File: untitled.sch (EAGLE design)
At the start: 9 parts, among them IC1 STM32F030F4P, X1 332-02, X2 332-04, X3 332-02, X4 332-02

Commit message: version 0.2
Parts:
- removed SV1: (no value), con-lstb:MA03-1
- added R2: (no value), rcl:R-EU_M1206
- added U1: GY-521MPU6050, gy-521:GY-521MPU6050
- added X5: 332-02, con-garry:332-02
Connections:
- net GND: now also X5-1.S; no longer SV1.1
- net N$10: now also R2.1, X5-2.S; no longer SV1.2
- net VCC: now also R2.2; no longer SV1.3
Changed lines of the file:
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@@
 <part name="SUPPLY5" library="supply2" deviceset="VCC" device=""/>
 <part name="X3" library="con-garry" deviceset="332-02" device=""/>
-<part name="SV1" library="con-lstb" deviceset="MA03-1" device=""/>
 <part name="GND5" library="supply1" deviceset="GND" device=""/>
 <part name="SUPPLY6" library="supply2" deviceset="VCC" device=""/>
 <part name="X4" library="con-garry" deviceset="332-02" device=""/>
 <part name="SUPPLY7" library="supply2" deviceset="VCC" device=""/>
+<part name="U1" library="gy-521" deviceset="GY-521" device="MPU6050"/>
+<part name="R2" library="rcl" deviceset="R-EU_" device="M1206"/>
+<part name="X5" library="con-garry" deviceset="332-02" device=""/>
 </parts>
 <sheets>
@@
 <instance part="X3" gate="-1" x="111.76" y="101.6"/>
 <instance part="X3" gate="-2" x="132.08" y="101.6"/>
-<instance part="SV1" gate="G$1" x="7.62" y="63.5" rot="R90"/>
 <instance part="GND5" gate="1" x="17.78" y="66.04"/>
 <instance part="SUPPLY6" gate="G$1" x="-15.24" y="76.2"/>
@@
 <instance part="X4" gate="-2" x="132.08" y="71.12"/>
 <instance part="SUPPLY7" gate="G$1" x="129.54" y="73.66"/>
+<instance part="U1" gate="G$1" x="193.04" y="139.7"/>
+<instance part="R2" gate="G$1" x="-5.08" y="73.66" rot="R180"/>
+<instance part="X5" gate="-1" x="10.16" y="68.58" rot="R270"/>
+<instance part="X5" gate="-2" x="7.62" y="68.58" rot="R270"/>
 </instances>
 <busses>
@@
 </segment>
 <segment>
-<pinref part="SV1" gate="G$1" pin="1"/>
 <pinref part="GND5" gate="1" pin="GND"/>
 <wire x1="10.16" y1="71.12" x2="17.78" y2="71.12" width="0.1524" layer="91"/>
 <wire x1="17.78" y1="71.12" x2="17.78" y2="68.58" width="0.1524" layer="91"/>
+<pinref part="X5" gate="-1" pin="S"/>
 </segment>
 </net>
@@
 </segment>
 <segment>
-<pinref part="SUPPLY6" gate="G$1" pin="VCC"/>
-<wire x1="-15.24" y1="73.66" x2="-15.24" y2="71.12" width="0.1524" layer="91"/>
-<pinref part="SV1" gate="G$1" pin="3"/>
-<wire x1="-15.24" y1="71.12" x2="5.08" y2="71.12" width="0.1524" layer="91"/>
-</segment>
-<segment>
 <pinref part="X4" gate="-2" pin="S"/>
 <pinref part="SUPPLY7" gate="G$1" pin="VCC"/>
+</segment>
+<segment>
+<pinref part="SUPPLY6" gate="G$1" pin="VCC"/>
+<pinref part="R2" gate="G$1" pin="2"/>
+<wire x1="-15.24" y1="73.66" x2="-10.16" y2="73.66" width="0.1524" layer="91"/>
 </segment>
 </net>
@@
 <segment>
 <pinref part="IC1" gate="MCU" pin="BOOT0"/>
-<pinref part="SV1" gate="G$1" pin="2"/>
 <wire x1="15.24" y1="78.74" x2="7.62" y2="78.74" width="0.1524" layer="91"/>
-<wire x1="7.62" y1="78.74" x2="7.62" y2="71.12" width="0.1524" layer="91"/>
-</segment>
-</net>
+<wire x1="7.62" y1="78.74" x2="7.62" y2="73.66" width="0.1524" layer="91"/>
+<pinref part="R2" gate="G$1" pin="1"/>
+<wire x1="7.62" y1="73.66" x2="7.62" y2="71.12" width="0.1524" layer="91"/>
+<wire x1="0" y1="73.66" x2="7.62" y2="73.66" width="0.1524" layer="91"/>
+<pinref part="X5" gate="-2" pin="S"/>
+</segment>
+</net>

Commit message: version 0.3 - proto 1
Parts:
- removed U$2: RFM69, RFM69mod:RFM69
- removed X1, X3, X4, X5: 332-02, con-garry:332-02
- removed X2: 332-04, con-garry:332-04
- added JP1: (no value), pinhead:PINHD-2X2
- added JP2, JP3, JP4, JP5: (no value), pinhead:PINHD-1X2
- added U2: RFM69CW, mike-temp:RFM69CW
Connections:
- removed net N$5: IC1MCU.PA6, U$2.MISO
- new net N$13: IC1MCU.PA5, U2.SCK
- net GND: now also JP1.2, JP2.2, JP5.1, U2.GND@1, U2.GND@2; no longer U$2.GND@1, X1-2.S, X2-2.S, X5-1.S
- net N$10: now also JP5.2; no longer X5-2.S
- net N$11: now also JP3.2; no longer X4-1.S
- net N$2: now also JP1.1; no longer X2-1.S
- net N$3: now also IC1MCU.PA6, U2.MISO; no longer IC1MCU.PA5, U$2.SCK
- net N$4: now also U2.NSS; no longer U$2.NSS
- net N$6: now also U2.MOSI; no longer U$2.MOSI
- net N$7: now also JP1.3; no longer X2-3.S
- net N$8: now also JP4.1; no longer X3-1.S
- net N$9: now also JP4.2; no longer X3-2.S
- net VCC: now also JP1.4, JP2.1, JP3.1, U2.3.3V; no longer U$2.3.3V, X1-1.S, X2-4.S, X4-2.S

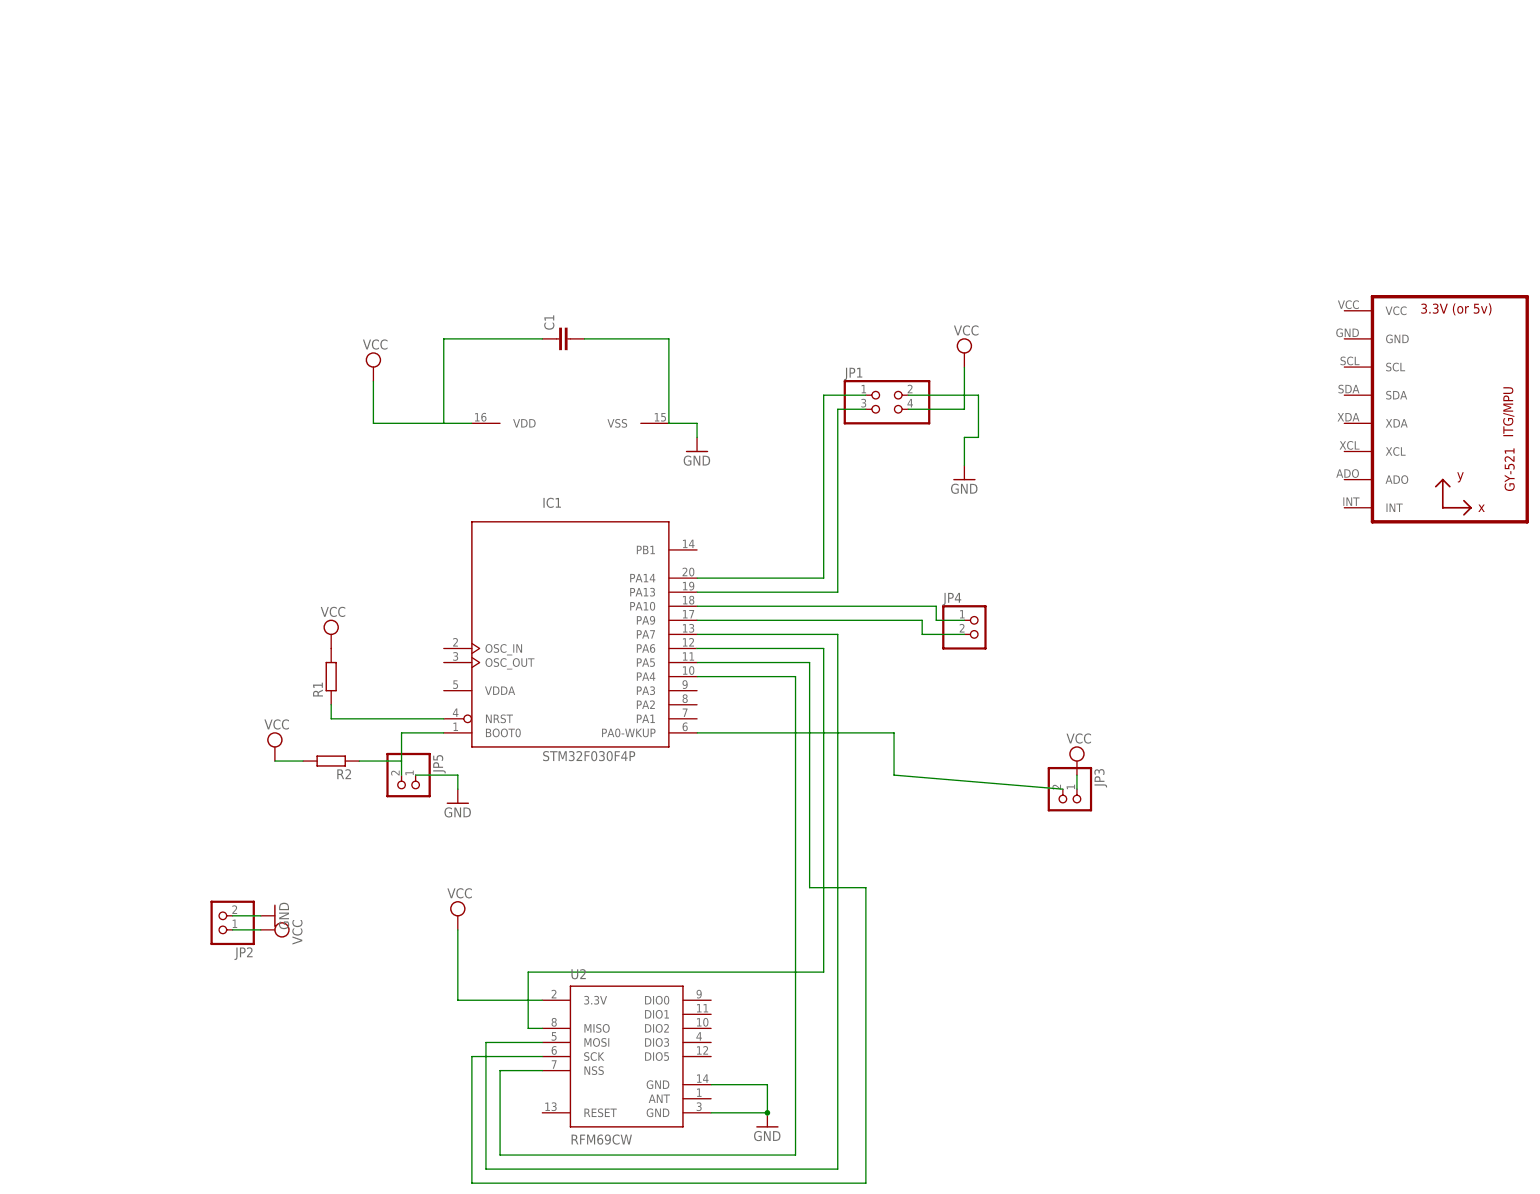
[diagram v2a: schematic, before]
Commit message: Change MCU to bigger version
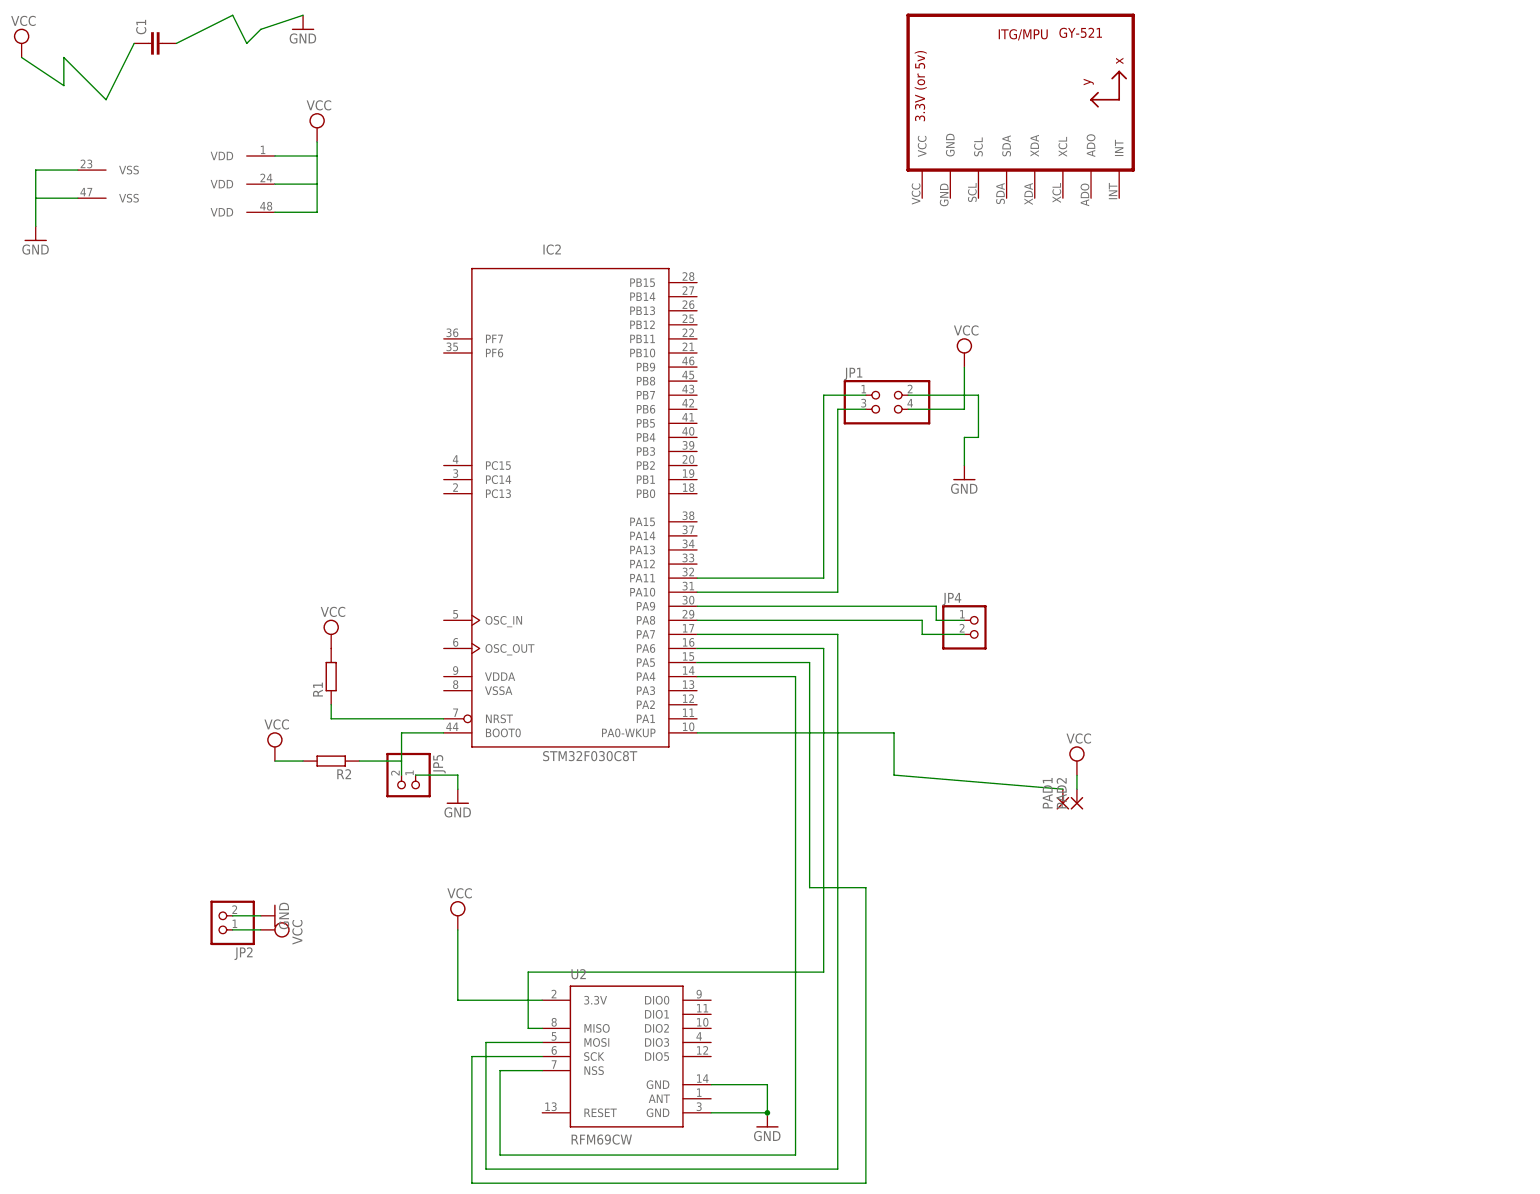
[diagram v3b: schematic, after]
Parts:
- removed IC1: STM32F030F4P, micro-stm_v2:STM32F030F4P
- removed JP3: (no value), pinhead:PINHD-1X2
- added IC2: STM32F030C8T, micro-stm_v2:STM32F030C8T
- added PAD1, PAD2: (no value), wirepad:SMD2
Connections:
- net GND: now also IC2PWR.VSS@1, IC2PWR.VSS@2; no longer IC1PWR.VSS@1
- net N$1: now also IC2MCU.NRST; no longer IC1MCU.NRST
- net N$10: now also IC2MCU.BOOT0; no longer IC1MCU.BOOT0
- net N$11: now also IC2MCU.PA0-WKUP, PAD1.P; no longer IC1MCU.PA0-WKUP, JP3.2
- net N$13: now also IC2MCU.PA5; no longer IC1MCU.PA5
- net N$2: now also IC2MCU.PA11; no longer IC1MCU.PA14
- net N$3: now also IC2MCU.PA6; no longer IC1MCU.PA6
- net N$4: now also IC2MCU.PA4; no longer IC1MCU.PA4
- net N$6: now also IC2MCU.PA7; no longer IC1MCU.PA7
- net N$7: now also IC2MCU.PA10; no longer IC1MCU.PA13
- net N$8: now also IC2MCU.PA9; no longer IC1MCU.PA10
- net N$9: now also IC2MCU.PA8; no longer IC1MCU.PA9
- net VCC: now also IC2PWR.VDD@1, IC2PWR.VDD@2, IC2PWR.VDD@3, PAD2.P; no longer IC1PWR.VDD@1, JP3.1
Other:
- moved on the sheet: C1
